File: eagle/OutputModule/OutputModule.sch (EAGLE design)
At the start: 26 parts, among them IC1 MCP23017SP

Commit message: 1.  Cleanup continues.  BlockController and the corresponding controller are deprecated along with SignalController and it's controller board.  These are replaced by the InputModule and OutputModule respectively 2.  TurnoutHandler moved to the MultiModuleController project folder 3.  Module moved to the MultiModuleController project folder 4.  More database cleanup work completed.
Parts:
- removed C1: (no value), SparkFun-Capacitors:CAPPTH
- added C2: 10uF, rcl:CPOL-EUE2.5-6
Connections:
- removed net INT: I2CIN.5, I2COUT.5, IC1.INTA
- new net VCC: I2CIN.3, I2COUT.3
- net +3V3: now also C2.+; no longer C1.2
- net GND: now also C2.-; no longer C1.1
- net SCL: now also I2CIN.4, I2COUT.4; no longer I2CIN.3, I2COUT.3
- net SDA: now also I2CIN.5, I2COUT.5; no longer I2CIN.4, I2COUT.4
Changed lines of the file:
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@@
 <part name="I2COUT" library="con-amp-quick" deviceset="M05" device="" value="PIN1"/>
 <part name="I2CIN" library="con-amp-quick" deviceset="M05" device="" value="PIN1"/>
-<part name="C1" library="SparkFun-Capacitors" deviceset="CAP" device="PTH"/>
 <part name="SW1" library="special" deviceset="SW_DIP-3" device=""/>
 <part name="R18" library="SparkFun-Passives" deviceset="RESISTOR" device="PTH-1/4W" value="10K"/>
 <part name="R19" library="SparkFun-Passives" deviceset="RESISTOR" device="PTH-1/4W" value="10K"/>
 <part name="R20" library="SparkFun-Passives" deviceset="RESISTOR" device="PTH-1/4W" value="10K"/>
+<part name="C2" library="rcl" deviceset="CPOL-EU" device="E2.5-6" value="10uF"/>
 </parts>
 <sheets>
@@
 <instance part="I2COUT" gate="G$1" x="12.7" y="101.6" rot="R270"/>
 <instance part="I2CIN" gate="G$1" x="30.48" y="12.7" rot="R180"/>
-<instance part="C1" gate="G$1" x="33.02" y="83.82" rot="R90"/>
 <instance part="SW1" gate="A" x="104.14" y="17.78"/>
 <instance part="R18" gate="G$1" x="48.26" y="12.7" rot="R90"/>
 <instance part="R19" gate="G$1" x="63.5" y="12.7" rot="R90"/>
 <instance part="R20" gate="G$1" x="78.74" y="12.7" rot="R90"/>
+<instance part="C2" gate="G$1" x="33.02" y="83.82" rot="R270"/>
 </instances>
 <busses>
 </busses>
 <nets>
-<net name="SCL" class="0">
-<segment>
-<wire x1="12.7" y1="93.98" x2="12.7" y2="55.88" width="0.1524" layer="91"/>
-<wire x1="12.7" y1="55.88" x2="12.7" y2="12.7" width="0.1524" layer="91"/>
-<wire x1="43.18" y1="55.88" x2="12.7" y2="55.88" width="0.1524" layer="91"/>
-<junction x="12.7" y="55.88"/>
+<net name="VCC" class="0">
+<segment>
+<wire x1="12.7" y1="93.98" x2="12.7" y2="12.7" width="0.1524" layer="91"/>
 <label x="12.7" y="86.36" size="1.778" layer="95" rot="R90"/>
-<pinref part="IC1" gate="G$1" pin="SCL"/>
 <pinref part="I2COUT" gate="G$1" pin="3"/>
 <pinref part="I2CIN" gate="G$1" pin="3"/>
@@
 </segment>
 </net>
-<net name="SDA" class="0">
+<net name="SCL" class="0">
 <segment>
 <label x="15.24" y="86.36" size="1.778" layer="95" rot="R90"/>
-<pinref part="IC1" gate="G$1" pin="SDA"/>
-<wire x1="15.24" y1="93.98" x2="15.24" y2="53.34" width="0.1524" layer="91"/>
-<wire x1="15.24" y1="53.34" x2="15.24" y2="10.16" width="0.1524" layer="91"/>
-<wire x1="43.18" y1="53.34" x2="15.24" y2="53.34" width="0.1524" layer="91"/>
-<junction x="15.24" y="53.34"/>
+<wire x1="15.24" y1="93.98" x2="15.24" y2="55.88" width="0.1524" layer="91"/>
 <pinref part="I2COUT" gate="G$1" pin="4"/>
+<wire x1="15.24" y1="55.88" x2="15.24" y2="10.16" width="0.1524" layer="91"/>
 <wire x1="22.86" y1="10.16" x2="15.24" y2="10.16" width="0.1524" layer="91"/>
 <pinref part="I2CIN" gate="G$1" pin="4"/>
-</segment>
-</net>
-<net name="INT" class="0">
+<pinref part="IC1" gate="G$1" pin="SCL"/>
+<wire x1="43.18" y1="55.88" x2="15.24" y2="55.88" width="0.1524" layer="91"/>
+<junction x="15.24" y="55.88"/>
+</segment>
+</net>
+<net name="SDA" class="0">
 <segment>
 <label x="17.78" y="86.36" size="1.778" layer="95" rot="R90"/>
-<wire x1="17.78" y1="93.98" x2="17.78" y2="68.58" width="0.1524" layer="91"/>
-<wire x1="17.78" y1="68.58" x2="17.78" y2="7.62" width="0.1524" layer="91"/>
-<wire x1="43.18" y1="68.58" x2="17.78" y2="68.58" width="0.1524" layer="91"/>
-<junction x="17.78" y="68.58"/>
-<pinref part="IC1" gate="G$1" pin="INTA"/>
+<wire x1="17.78" y1="93.98" x2="17.78" y2="53.34" width="0.1524" layer="91"/>
+<wire x1="17.78" y1="53.34" x2="17.78" y2="7.62" width="0.1524" layer="91"/>
 <pinref part="I2COUT" gate="G$1" pin="5"/>
 <wire x1="22.86" y1="7.62" x2="17.78" y2="7.62" width="0.1524" layer="91"/>
 <pinref part="I2CIN" gate="G$1" pin="5"/>
+<pinref part="IC1" gate="G$1" pin="SDA"/>
+<wire x1="43.18" y1="53.34" x2="17.78" y2="53.34" width="0.1524" layer="91"/>
+<junction x="17.78" y="53.34"/>
 </segment>
 </net>
@@
 <pinref part="I2CIN" gate="G$1" pin="1"/>
 <wire x1="22.86" y1="17.78" x2="7.62" y2="17.78" width="0.1524" layer="91"/>
-<pinref part="C1" gate="G$1" pin="1"/>
 <wire x1="27.94" y1="83.82" x2="7.62" y2="83.82" width="0.1524" layer="91"/>
 <junction x="7.62" y="83.82"/>
@@
 <wire x1="40.64" y1="33.02" x2="33.02" y2="33.02" width="0.1524" layer="91"/>
 <junction x="33.02" y="33.02"/>
+<pinref part="C2" gate="G$1" pin="-"/>
 </segment>
 </net>
@@
 <pinref part="I2CIN" gate="G$1" pin="2"/>
 <wire x1="22.86" y1="15.24" x2="10.16" y2="15.24" width="0.1524" layer="91"/>
-<pinref part="C1" gate="G$1" pin="2"/>
 <wire x1="35.56" y1="83.82" x2="38.1" y2="83.82" width="0.1524" layer="91"/>
 <wire x1="38.1" y1="83.82" x2="38.1" y2="78.74" width="0.1524" layer="91"/>
@@
 <wire x1="10.16" y1="2.54" x2="10.16" y2="15.24" width="0.1524" layer="91"/>
 <junction x="10.16" y="15.24"/>
-</segment>
-</net>
+<pinref part="C2" gate="G$1" pin="+"/>
+</segment>
+</net>

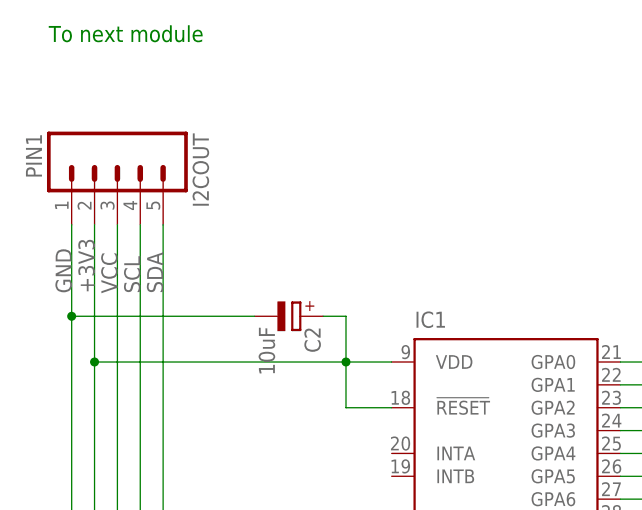
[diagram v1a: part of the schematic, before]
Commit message: 1.  Cleanup work 2.  Reduced the retry timeout to 2 seconds (from 3) 3.  Change the TurnoutModule board to use the same address pins as the other modules 4.  Add a two-pin header to Input and Output module boards with access to GND and 3.3v 5.  Move the call to module->finishxxx to before network setup code so that the modules can initialize while the network connection is being established
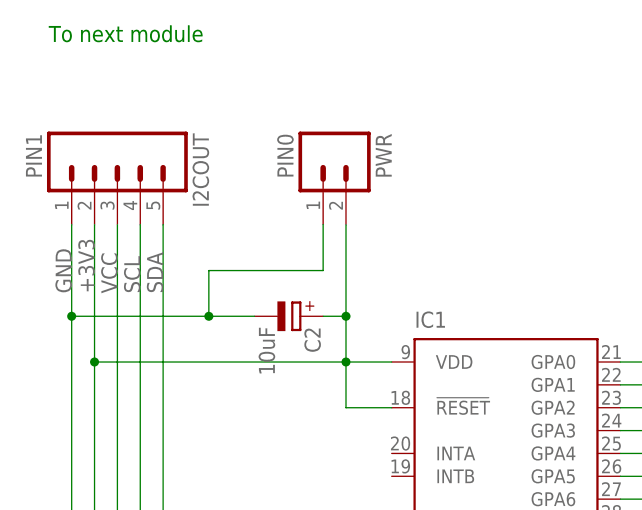
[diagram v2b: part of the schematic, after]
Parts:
- added PWR: PIN0, con-amp-quick:M02
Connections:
- net +3V3: now also PWR.2
- net GND: now also PWR.1
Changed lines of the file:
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@@
 <part name="R20" library="SparkFun-Passives" deviceset="RESISTOR" device="PTH-1/4W" value="10K"/>
 <part name="C2" library="rcl" deviceset="CPOL-EU" device="E2.5-6" value="10uF"/>
+<part name="PWR" library="con-amp-quick" deviceset="M02" device="" value="PIN0"/>
 </parts>
 <sheets>
@@
 <instance part="R20" gate="G$1" x="78.74" y="12.7" rot="R90"/>
 <instance part="C2" gate="G$1" x="33.02" y="83.82" rot="R270"/>
+<instance part="PWR" gate="G$1" x="35.56" y="101.6" rot="R270"/>
 </instances>
 <busses>
@@
 <pinref part="I2CIN" gate="G$1" pin="1"/>
 <wire x1="22.86" y1="17.78" x2="7.62" y2="17.78" width="0.1524" layer="91"/>
-<wire x1="27.94" y1="83.82" x2="7.62" y2="83.82" width="0.1524" layer="91"/>
+<wire x1="27.94" y1="83.82" x2="22.86" y2="83.82" width="0.1524" layer="91"/>
 <junction x="7.62" y="83.82"/>
 <pinref part="R20" gate="G$1" pin="1"/>
+<wire x1="22.86" y1="83.82" x2="7.62" y2="83.82" width="0.1524" layer="91"/>
 <wire x1="78.74" y1="5.08" x2="78.74" y2="7.62" width="0.1524" layer="91"/>
 <wire x1="63.5" y1="5.08" x2="78.74" y2="5.08" width="0.1524" layer="91"/>
@@
 <junction x="33.02" y="33.02"/>
 <pinref part="C2" gate="G$1" pin="-"/>
+<wire x1="22.86" y1="83.82" x2="22.86" y2="88.9" width="0.1524" layer="91"/>
+<junction x="22.86" y="83.82"/>
+<pinref part="PWR" gate="G$1" pin="1"/>
+<wire x1="22.86" y1="88.9" x2="35.56" y2="88.9" width="0.1524" layer="91"/>
+<wire x1="35.56" y1="88.9" x2="35.56" y2="93.98" width="0.1524" layer="91"/>
 </segment>
 </net>
@@
 <junction x="10.16" y="15.24"/>
 <pinref part="C2" gate="G$1" pin="+"/>
-</segment>
-</net>
+<pinref part="PWR" gate="G$1" pin="2"/>
+<wire x1="38.1" y1="93.98" x2="38.1" y2="83.82" width="0.1524" layer="91"/>
+<junction x="38.1" y="83.82"/>
+</segment>
+</net>
